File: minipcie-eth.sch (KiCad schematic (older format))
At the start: 7 parts, among them J1 UART2, U1 VoCore_v2

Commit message: Move libs away from rescue. Re-constrained board layout since cutouts were not perpendicular (overconstrained)
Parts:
- removed J1: UART2, KiCad/Pin_Headers.pretty:Pin_Header_Straight_1x04_Pitch2.54mm, symbol minipcie-eth-rescue:Conn_01x04
- J2: renamed from J?; footprint (none) -> Connector_PinHeader_2.54mm:PinHeader_2x06_P2.54mm_Vertical
- U1: footprint win:VoCore_v2 -> vocore2:VOCORE2; symbol minipcie-eth-rescue:VoCore_v2-win -> vocore_v2-win:VoCore_v2-win
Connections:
- wire segments 95 -> 89
- no-connect marks 22 -> 24
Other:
- note added: "XXX: PMOD expanded SPI (type 2A) should offer the highest flexibility?"
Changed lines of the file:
@@
 $EndDescr
 $Comp
-L minipcie-eth-rescue:VoCore_v2-win U1
+L vocore_v2-win:VoCore_v2-win U1
 U 1 1 5BAF0D89
 P 5710 3930
-F 0 "U1" H 6820 5140 50  0000 C CNN
-F 1 "VoCore_v2" H 6670 5230 50  0000 C CNN
-F 2 "win:VoCore_v2" H 5710 3580 50  0001 C CNN
-F 3 "DOCUMENTATION" H 5710 3480 50  0001 C CNN
+F 0 "U1" H 5710 3980 50  0000 C CNN
+F 1 "VoCore_v2" H 5710 3880 50  0000 C CNN
+F 2 "vocore2:VOCORE2" H 5710 3580 50  0001 C CNN
+F 3 "" H 5710 3480 50  0001 C CNN
 	1    5710 3930
 	1    0    0    -1
@@
 F0 "ethernet + POE" 60
 F1 "ethernet.sch" 60
-F2 "P0RN" I R 2700 3580 60
-F3 "P0RP" I R 2700 3480 60
-F4 "P0TP" I R 2700 3680 60
-F5 "P0TN" I R 2700 3780 60
+F2 "PORN" I R 2700 3580 60
+F3 "PORP" I R 2700 3480 60
+F4 "POTP" I R 2700 3680 60
+F5 "POTN" I R 2700 3780 60
 F6 "5V+_POE" I L 1860 4210 60
 F7 "5V-_POE" I L 1860 4330 60
@@
 $EndSheet
 $Comp
-L minipcie-eth-rescue:Conn_01x04 J1
-U 1 1 5BAF1493
-P 3770 4370
-F 0 "J1" H 3890 4560 50  0000 C CNN
-F 1 "UART2" H 3960 4480 50  0000 C CNN
-F 2 "KiCad/Pin_Headers.pretty:Pin_Header_Straight_1x04_Pitch2.54mm" H 3770 4370 50  0001 C CNN
-F 3 "" H 3770 4370 50  0001 C CNN
-	1    3770 4370
-	-1   0    0    1
-$EndComp
-$Comp
 L power1:GND #PWR01
 U 1 1 5BAF1546
@@
 F 3 "" H 6160 5530 50  0001 C CNN
 	1    6160 5530
-	-1   0    0    1
-$EndComp
-$Comp
-L power1:+5V #PWR06
-U 1 1 5BAF2AC1
-P 3970 4470
-F 0 "#PWR06" H 3970 4320 50  0001 C CNN
-F 1 "+5V" H 3985 4643 50  0000 C CNN
-F 2 "" H 3970 4470 50  0001 C CNN
-F 3 "" H 3970 4470 50  0001 C CNN
-	1    3970 4470
-	-1   0    0    1
-$EndComp
-$Comp
-L power1:GND #PWR07
-U 1 1 5BAF2AD4
-P 3970 4170
-F 0 "#PWR07" H 3970 3920 50  0001 C CNN
-F 1 "GND" H 3975 3997 50  0000 C CNN
-F 2 "" H 3970 4170 50  0001 C CNN
-F 3 "" H 3970 4170 50  0001 C CNN
-	1    3970 4170
 	-1   0    0    1
 $EndComp
@@
 	7160 3430 7550 3430
 Wire Wire Line
-	4260 3980 4120 3980
-Wire Wire Line
-	4120 3980 4120 4370
-Wire Wire Line
-	4120 4370 3970 4370
-Wire Wire Line
-	4260 3880 4050 3880
-Wire Wire Line
-	4050 3880 4050 4270
-Wire Wire Line
-	4050 4270 3970 4270
-Wire Wire Line
 	5860 5380 5860 5950
 Wire Wire Line
@@
 	5160 2390 5160 2480
 $Comp
-L power:VBUS #PWR?
+L power:VBUS #PWR0101
 U 1 1 5C95EBC9
 P 8990 4580
-F 0 "#PWR?" H 8990 4430 50  0001 C CNN
+F 0 "#PWR0101" H 8990 4430 50  0001 C CNN
 F 1 "VBUS" H 9005 4753 50  0000 C CNN
 F 2 "" H 8990 4580 50  0001 C CNN
@@
 $EndComp
 $Comp
-L Connector_Generic:Conn_02x06_Top_Bottom J?
+L Connector_Generic:Conn_02x06_Top_Bottom J2
 U 1 1 5C96207F
 P 8690 4280
-F 0 "J?" H 8740 4697 50  0000 C CNN
+F 0 "J2" H 8740 4697 50  0000 C CNN
 F 1 "POE PMOD" H 8740 4606 50  0000 C CNN
-F 2 "" H 8690 4280 50  0001 C CNN
+F 2 "Connector_PinHeader_2.54mm:PinHeader_2x06_P2.54mm_Vertical" H 8690 4280 50  0001 C CNN
 F 3 "~" H 8690 4280 50  0001 C CNN
 	1    8690 4280
@@
 $EndComp
 $Comp
-L power:VBUS #PWR?
+L power:VBUS #PWR0102
 U 1 1 5C9740EC
 P 8490 4580
-F 0 "#PWR?" H 8490 4430 50  0001 C CNN
+F 0 "#PWR0102" H 8490 4430 50  0001 C CNN
 F 1 "VBUS" H 8505 4753 50  0000 C CNN
 F 2 "" H 8490 4580 50  0001 C CNN
@@
 $EndComp
 $Comp
-L power:GNDA #PWR?
+L power:GNDA #PWR0103
 U 1 1 5C97B896
 P 8990 4480
-F 0 "#PWR?" H 8990 4230 50  0001 C CNN
+F 0 "#PWR0103" H 8990 4230 50  0001 C CNN
 F 1 "GNDA" V 8995 4352 50  0000 R CNN
 F 2 "" H 8990 4480 50  0001 C CNN
@@
 $EndComp
 $Comp
-L power:GNDA #PWR?
+L power:GNDA #PWR0104
 U 1 1 5C97C16E
 P 8490 4480
-F 0 "#PWR?" H 8490 4230 50  0001 C CNN
+F 0 "#PWR0104" H 8490 4230 50  0001 C CNN
 F 1 "GNDA" V 8495 4353 50  0000 R CNN
 F 2 "" H 8490 4480 50  0001 C CNN
@@
 	0    1    1    0
 $EndComp
+NoConn ~ 4260 3880
+NoConn ~ 4260 3980
+Text Notes 8440 5050 0    60   ~ 0
+XXX: PMOD expanded SPI (type 2A) should offer the highest flexibility?
 $EndSCHEMATC

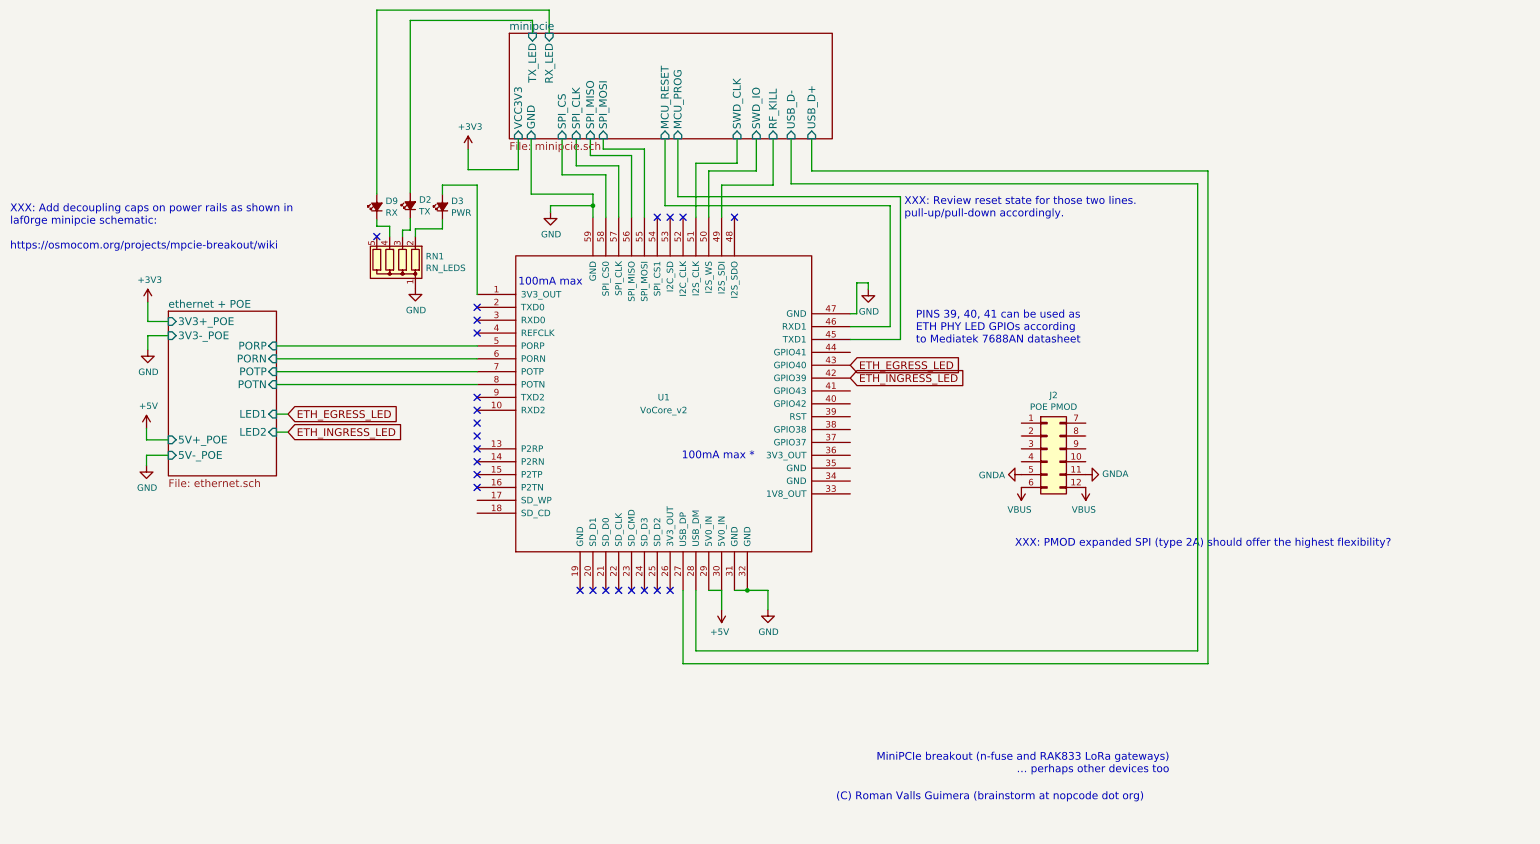
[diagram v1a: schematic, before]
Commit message: Added PMOD 6 header pins, mouse bites, copper fills for main board
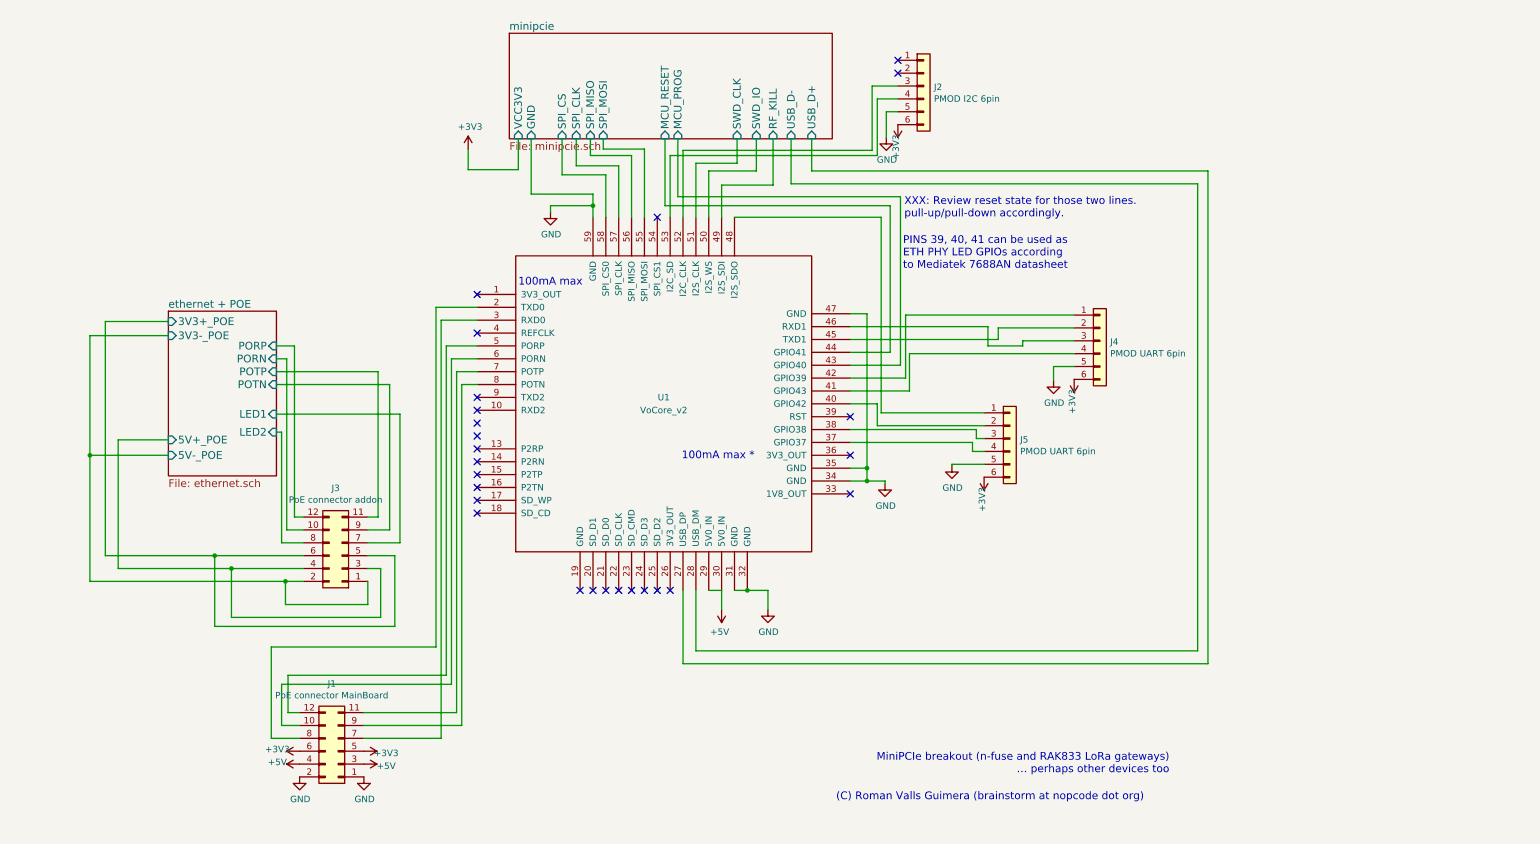
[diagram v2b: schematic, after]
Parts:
- removed D2: TX, KiCad/Diodes_SMD.pretty:D_0603, symbol device1:LED_Small_ALT
- removed D3: PWR, KiCad/Diodes_SMD.pretty:D_0603, symbol device1:LED_Small_ALT
- removed D9: RX, KiCad/Diodes_SMD.pretty:D_0603, symbol device1:LED_Small_ALT
- removed J2: POE PMOD, Connector_PinHeader_2.54mm:PinHeader_2x06_P2.54mm_Vertical, symbol Connector_Generic:Conn_02x06_Top_Bottom
- removed RN1: RN_LEDS, KiCad/Resistors_SMD.pretty:R_Array_Concave_4x0603, symbol device1:R_Network04
- added J1: PoE connector MainBoard, Connector_PinHeader_2.54mm:PinHeader_2x06_P2.54mm_Vertical, symbol Connector_Generic:Conn_02x06_Odd_Even
- added J2: PMOD I2C 6pin, Connector_PinHeader_2.54mm:PinHeader_1x06_P2.54mm_Horizontal, symbol Connector_Generic:Conn_01x06
- added J3: PoE connector addon, Connector_PinHeader_2.54mm:PinHeader_2x06_P2.54mm_Vertical, symbol Connector_Generic:Conn_02x06_Odd_Even
- added J4, J5: PMOD UART 6pin, Connector_PinHeader_2.54mm:PinHeader_1x06_P2.54mm_Horizontal, symbol Connector_Generic:Conn_01x06
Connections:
- net ETH_EGRESS_LED is gone; now on net minipcie/MCU_PROG: U1.43 (GPIO40)
- net +3V3: now also J1.5 (Pin_5), J1.6 (Pin_6), J2.6 (Pin_6), J4.6 (Pin_6), J5.6 (Pin_6)
- net +5V: now also J1.3 (Pin_3), J1.4 (Pin_4)
- net GND: now also U1.34 (GND), U1.35 (GND), J1.1 (Pin_1), J1.2 (Pin_2), J2.5 (Pin_5), J4.5 (Pin_5), J5.5 (Pin_5)
- net ethernet + POE/PORN: now also J3.10 (Pin_10); no longer U1.6 (PORN)
- net ethernet + POE/PORP: now also J3.12 (Pin_12); no longer U1.5 (PORP)
- net ethernet + POE/POTN: now also J3.9 (Pin_9); no longer U1.8 (POTN)
- net ethernet + POE/POTP: now also J3.11 (Pin_11); no longer U1.7 (POTP)
- net minipcie/MCU_PROG: no longer U1.45 (TXD1)
- net minipcie/MCU_RESET: now also U1.44 (GPIO41); no longer U1.46 (RXD1)
- net at U1.2 (TXD0): now also J1.8 (Pin_8)
- net at U1.3 (RXD0): now also J1.7 (Pin_7)
- net at U1.37 (GPIO37): now also J5.4 (Pin_4)
- net at U1.38 (GPIO38): now also J5.3 (Pin_3)
- net at U1.40 (GPIO42): now also J5.2 (Pin_2)
- net at U1.41 (GPIO43): now also J4.4 (Pin_4)
- net at U1.48 (I2S_SDO): now also J5.1 (Pin_1)
- net at U1.52 (I2C_CLK): now also J2.3 (Pin_3)
- net at U1.53 (I2C_SD): now also J2.4 (Pin_4)
- net ETH_INGRESS_LED: no longer names the net of U1.42 (GPIO39)
- net ETH_INGRESS_LED: now also J4.1 (Pin_1)
- new net: J4.2 (Pin_2), U1.45 (TXD1)
- new net: J4.3 (Pin_3), U1.46 (RXD1)
- new net: J1.12 (Pin_12), U1.5 (PORP)
- new net: J1.10 (Pin_10), U1.6 (PORN)
- new net: J1.11 (Pin_11), U1.7 (POTP)
- new net: J1.9 (Pin_9), U1.8 (POTN)
- new net ethernet + POE/3V3+_POE: J3.5 (Pin_5), J3.6 (Pin_6)
- new net ethernet + POE/3V3-_POE: J3.1 (Pin_1), J3.2 (Pin_2)
- new net ethernet + POE/5V+_POE: J3.3 (Pin_3), J3.4 (Pin_4)
- new net ethernet + POE/LED1: J3.7 (Pin_7)
- new net ethernet + POE/LED2: J3.8 (Pin_8)
- no-connect marks 24 -> 26
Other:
- note removed: "XXX: Add decoupling caps on power rails as shown in\nlaf0rge minipcie schematic:\n\nhttps://osmocom.org/projects/mpcie-breakout/wiki"
- note removed: "XXX: PMOD expanded SPI (type 2A) should offer the highest flexibility?"

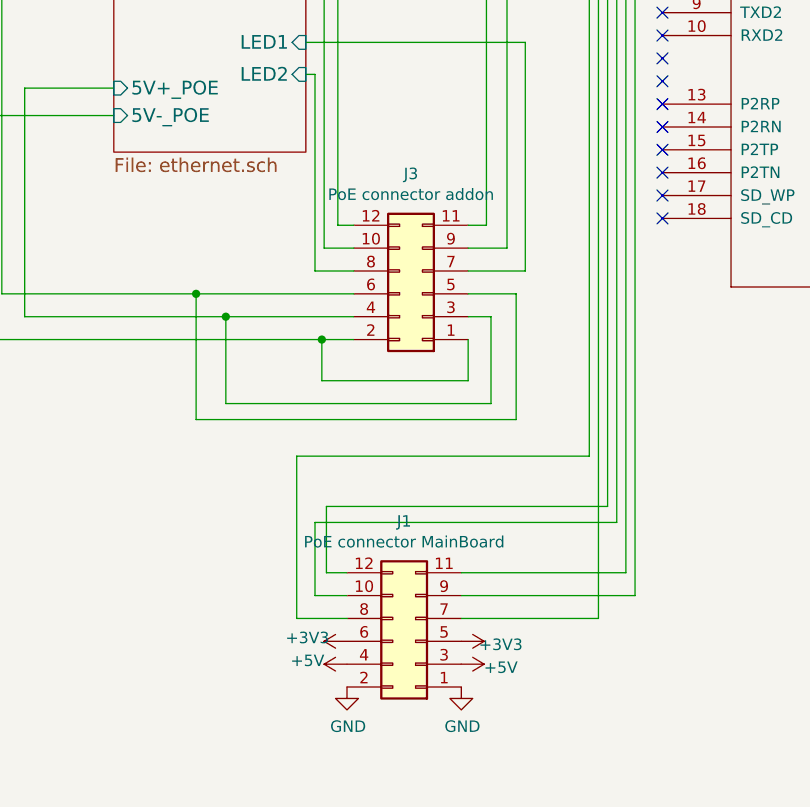
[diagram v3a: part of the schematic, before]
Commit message: Switch to 90 degree orientation of the VoCore2. Separate 2.54mm pin headers into two 6-pin connectors, separating data and power, ready to re-route
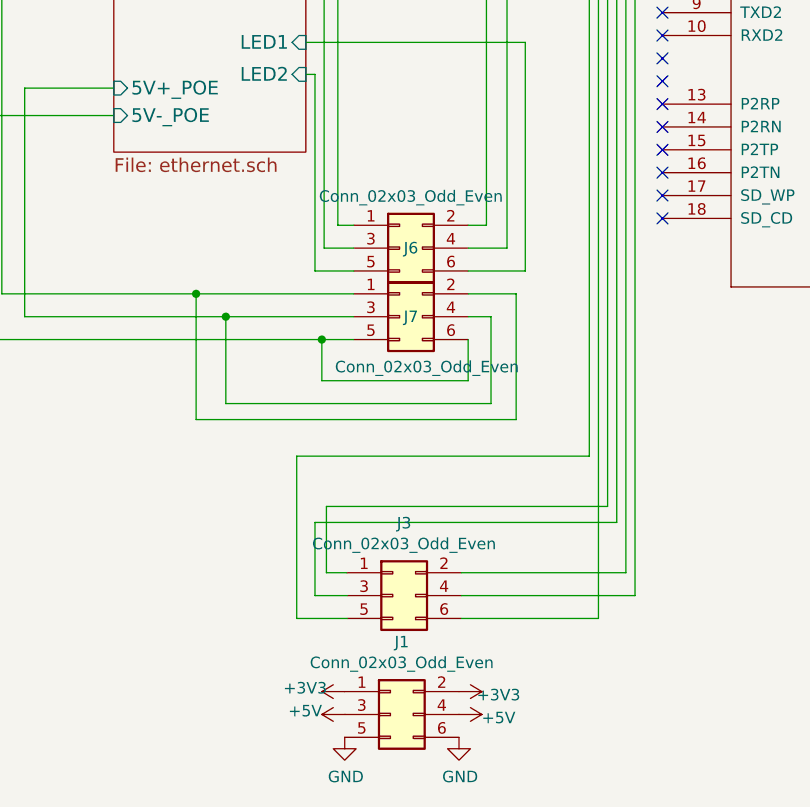
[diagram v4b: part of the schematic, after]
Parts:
- removed J1: PoE connector MainBoard, Connector_PinHeader_2.54mm:PinHeader_2x06_P2.54mm_Vertical, symbol Connector_Generic:Conn_02x06_Odd_Even
- removed J3: PoE connector addon, Connector_PinHeader_2.54mm:PinHeader_2x06_P2.54mm_Vertical, symbol Connector_Generic:Conn_02x06_Odd_Even
- added J1, J3, J6, J7: Conn_02x03_Odd_Even, Connector_PinHeader_2.54mm:PinHeader_2x03_P2.54mm_Vertical, symbol Connector_Generic:Conn_02x03_Odd_Even
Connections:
- net +3V3: now also J1.1 (Pin_1), J1.2 (Pin_2)
- net +5V: now also J1.3 (Pin_3), J1.4 (Pin_4)
- net GND: now also J1.5 (Pin_5), J1.6 (Pin_6)
- net ethernet + POE/3V3+_POE: now also J7.1 (Pin_1), J7.2 (Pin_2)
- net ethernet + POE/3V3-_POE: now also J7.5 (Pin_5), J7.6 (Pin_6)
- net ethernet + POE/5V+_POE: now also J7.3 (Pin_3), J7.4 (Pin_4)
- net ethernet + POE/LED1: now also J6.6 (Pin_6)
- net ethernet + POE/LED2: now also J6.5 (Pin_5)
- net ethernet + POE/PORN: now also J6.3 (Pin_3)
- net ethernet + POE/PORP: now also J6.1 (Pin_1)
- net ethernet + POE/POTN: now also J6.4 (Pin_4)
- net ethernet + POE/POTP: now also J6.2 (Pin_2)
- net at U1.2 (TXD0): now also J3.5 (Pin_5)
- net at U1.3 (RXD0): now also J3.6 (Pin_6)
- net at U1.5 (PORP): now also J3.1 (Pin_1)
- net at U1.6 (PORN): now also J3.3 (Pin_3)
- net at U1.7 (POTP): now also J3.2 (Pin_2)
- net at U1.8 (POTN): now also J3.4 (Pin_4)
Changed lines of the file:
@@
 NoConn ~ 4260 4680
 NoConn ~ 4260 4780
-$Comp
-L Connector_Generic:Conn_02x06_Odd_Even J3
-U 1 1 5CBE4AC9
-P 3210 5110
-F 0 "J3" H 3260 4585 50  0000 C CNN
-F 1 "PoE connector addon" H 3260 4676 50  0000 C CNN
-F 2 "Connector_PinHeader_2.54mm:PinHeader_2x06_P2.54mm_Vertical" H 3210 5110 50  0001 C CNN
-F 3 "~" H 3210 5110 50  0001 C CNN
-	1    3210 5110
-	-1   0    0    1
-$EndComp
-$Comp
-L Connector_Generic:Conn_02x06_Odd_Even J1
-U 1 1 5CC3D096
-P 3180 6630
-F 0 "J1" H 3230 6105 50  0000 C CNN
-F 1 "PoE connector MainBoard" H 3230 6196 50  0000 C CNN
-F 2 "Connector_PinHeader_2.54mm:PinHeader_2x06_P2.54mm_Vertical" H 3180 6630 50  0001 C CNN
-F 3 "~" H 3180 6630 50  0001 C CNN
-	1    3180 6630
-	-1   0    0    1
-$EndComp
 Connection ~ 6360 5380
 Wire Wire Line
@@
 L power1:GND #PWR0111
 U 1 1 5CD4BE9C
-P 2880 6830
-F 0 "#PWR0111" H 2880 6580 50  0001 C CNN
-F 1 "GND" H 2885 6657 50  0000 C CNN
-F 2 "" H 2880 6830 50  0001 C CNN
-F 3 "" H 2880 6830 50  0001 C CNN
-	1    2880 6830
+P 2870 7050
+F 0 "#PWR0111" H 2870 6800 50  0001 C CNN
+F 1 "GND" H 2875 6877 50  0000 C CNN
+F 2 "" H 2870 7050 50  0001 C CNN
+F 3 "" H 2870 7050 50  0001 C CNN
+	1    2870 7050
 	1    0    0    -1
 $EndComp
@@
 L power1:GND #PWR0112
 U 1 1 5CD4C2C5
-P 3380 6830
-F 0 "#PWR0112" H 3380 6580 50  0001 C CNN
-F 1 "GND" H 3385 6657 50  0000 C CNN
-F 2 "" H 3380 6830 50  0001 C CNN
-F 3 "" H 3380 6830 50  0001 C CNN
-	1    3380 6830
+P 3370 7050
+F 0 "#PWR0112" H 3370 6800 50  0001 C CNN
+F 1 "GND" H 3375 6877 50  0000 C CNN
+F 2 "" H 3370 7050 50  0001 C CNN
+F 3 "" H 3370 7050 50  0001 C CNN
+	1    3370 7050
 	1    0    0    -1
 $EndComp
@@
 L power1:+3V3 #PWR0115
 U 1 1 5CE3B0C3
-P 2880 6630
-F 0 "#PWR0115" H 2880 6480 50  0001 C CNN
-F 1 "+3V3" V 2895 6803 50  0000 C CNN
-F 2 "" H 2880 6630 50  0001 C CNN
-F 3 "" H 2880 6630 50  0001 C CNN
-	1    2880 6630
+P 2870 6850
+F 0 "#PWR0115" H 2870 6700 50  0001 C CNN
+F 1 "+3V3" V 2885 7023 50  0000 C CNN
+F 2 "" H 2870 6850 50  0001 C CNN
+F 3 "" H 2870 6850 50  0001 C CNN
+	1    2870 6850
 	0    -1   -1   0
 $EndComp
@@
 L power1:+3V3 #PWR0116
 U 1 1 5CE3BC83
-P 3380 6630
-F 0 "#PWR0116" H 3380 6480 50  0001 C CNN
-F 1 "+3V3" V 3395 6803 50  0000 C CNN
-F 2 "" H 3380 6630 50  0001 C CNN
-F 3 "" H 3380 6630 50  0001 C CNN
-	1    3380 6630
+P 3370 6850
+F 0 "#PWR0116" H 3370 6700 50  0001 C CNN
+F 1 "+3V3" V 3385 7023 50  0000 C CNN
+F 2 "" H 3370 6850 50  0001 C CNN
+F 3 "" H 3370 6850 50  0001 C CNN
+	1    3370 6850
 	0    1    1    0
 $EndComp
@@
 L power1:+5V #PWR0114
 U 1 1 5CD58DDB
-P 3380 6730
-F 0 "#PWR0114" H 3380 6580 50  0001 C CNN
-F 1 "+5V" V 3395 6903 50  0000 C CNN
-F 2 "" H 3380 6730 50  0001 C CNN
-F 3 "" H 3380 6730 50  0001 C CNN
-	1    3380 6730
+P 3370 6950
+F 0 "#PWR0114" H 3370 6800 50  0001 C CNN
+F 1 "+5V" V 3385 7123 50  0000 C CNN
+F 2 "" H 3370 6950 50  0001 C CNN
+F 3 "" H 3370 6950 50  0001 C CNN
+	1    3370 6950
 	0    1    1    0
 $EndComp
@@
 L power1:+5V #PWR0113
 U 1 1 5CD4C81C
-P 2880 6730
-F 0 "#PWR0113" H 2880 6580 50  0001 C CNN
-F 1 "+5V" V 2895 6903 50  0000 C CNN
-F 2 "" H 2880 6730 50  0001 C CNN
-F 3 "" H 2880 6730 50  0001 C CNN
-	1    2880 6730
+P 2870 6950
+F 0 "#PWR0113" H 2870 6800 50  0001 C CNN
+F 1 "+5V" V 2885 7123 50  0000 C CNN
+F 2 "" H 2870 6950 50  0001 C CNN
+F 3 "" H 2870 6950 50  0001 C CNN
+	1    2870 6950
 	0    -1   -1   0
 $EndComp
@@
 Wire Wire Line
 	1860 3400 1250 3400
+$Comp
+L Connector_Generic:Conn_02x03_Odd_Even J3
+U 1 1 5D4C6E7B
+P 3080 6430
+F 0 "J3" H 3130 6747 50  0000 C CNN
+F 1 "Conn_02x03_Odd_Even" H 3130 6656 50  0000 C CNN
+F 2 "Connector_PinHeader_2.54mm:PinHeader_2x03_P2.54mm_Vertical" H 3080 6430 50  0001 C CNN
+F 3 "~" H 3080 6430 50  0001 C CNN
+	1    3080 6430
+	1    0    0    -1
+$EndComp
+$Comp
+L Connector_Generic:Conn_02x03_Odd_Even J1
+U 1 1 5D4C7761
+P 3070 6950
+F 0 "J1" H 3120 7267 50  0000 C CNN
+F 1 "Conn_02x03_Odd_Even" H 3120 7176 50  0000 C CNN
+F 2 "Connector_PinHeader_2.54mm:PinHeader_2x03_P2.54mm_Vertical" H 3070 6950 50  0001 C CNN
+F 3 "~" H 3070 6950 50  0001 C CNN
+	1    3070 6950
+	1    0    0    -1
+$EndComp
+$Comp
+L Connector_Generic:Conn_02x03_Odd_Even J7
+U 1 1 5D4DD4EF
+P 3110 5210
+F 0 "J7" H 3160 5210 50  0000 C CNN
+F 1 "Conn_02x03_Odd_Even" H 3230 4990 50  0000 C CNN
+F 2 "Connector_PinHeader_2.54mm:PinHeader_2x03_P2.54mm_Vertical" H 3110 5210 50  0001 C CNN
+F 3 "~" H 3110 5210 50  0001 C CNN
+	1    3110 5210
+	1    0    0    -1
+$EndComp
+$Comp
+L Connector_Generic:Conn_02x03_Odd_Even J6
+U 1 1 5D4DE63D
+P 3110 4910
+F 0 "J6" H 3160 4910 50  0000 C CNN
+F 1 "Conn_02x03_Odd_Even" H 3160 5136 50  0000 C CNN
+F 2 "Connector_PinHeader_2.54mm:PinHeader_2x03_P2.54mm_Vertical" H 3110 4910 50  0001 C CNN
+F 3 "~" H 3110 4910 50  0001 C CNN
+	1    3110 4910
+	1    0    0    -1
+$EndComp
 $EndSCHEMATC
